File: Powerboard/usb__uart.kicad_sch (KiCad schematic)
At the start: 24 parts, among them IC2 CP2102, J8 USB_C_Receptacle_USB2.0, U10 RT9025-25GSP, U11 LTC4411

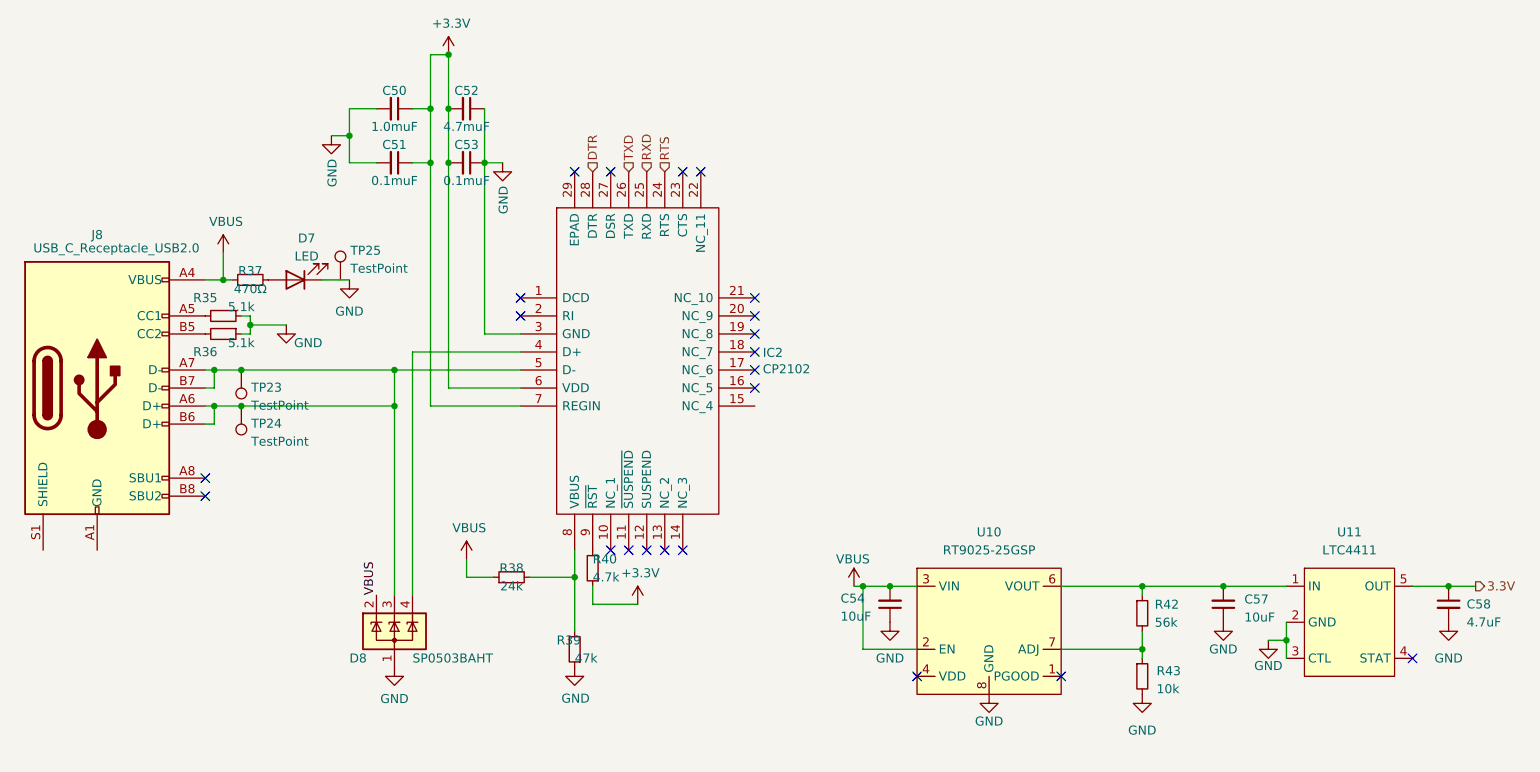
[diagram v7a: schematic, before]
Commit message: grouped components by circuit, done CAN transceiver layout.
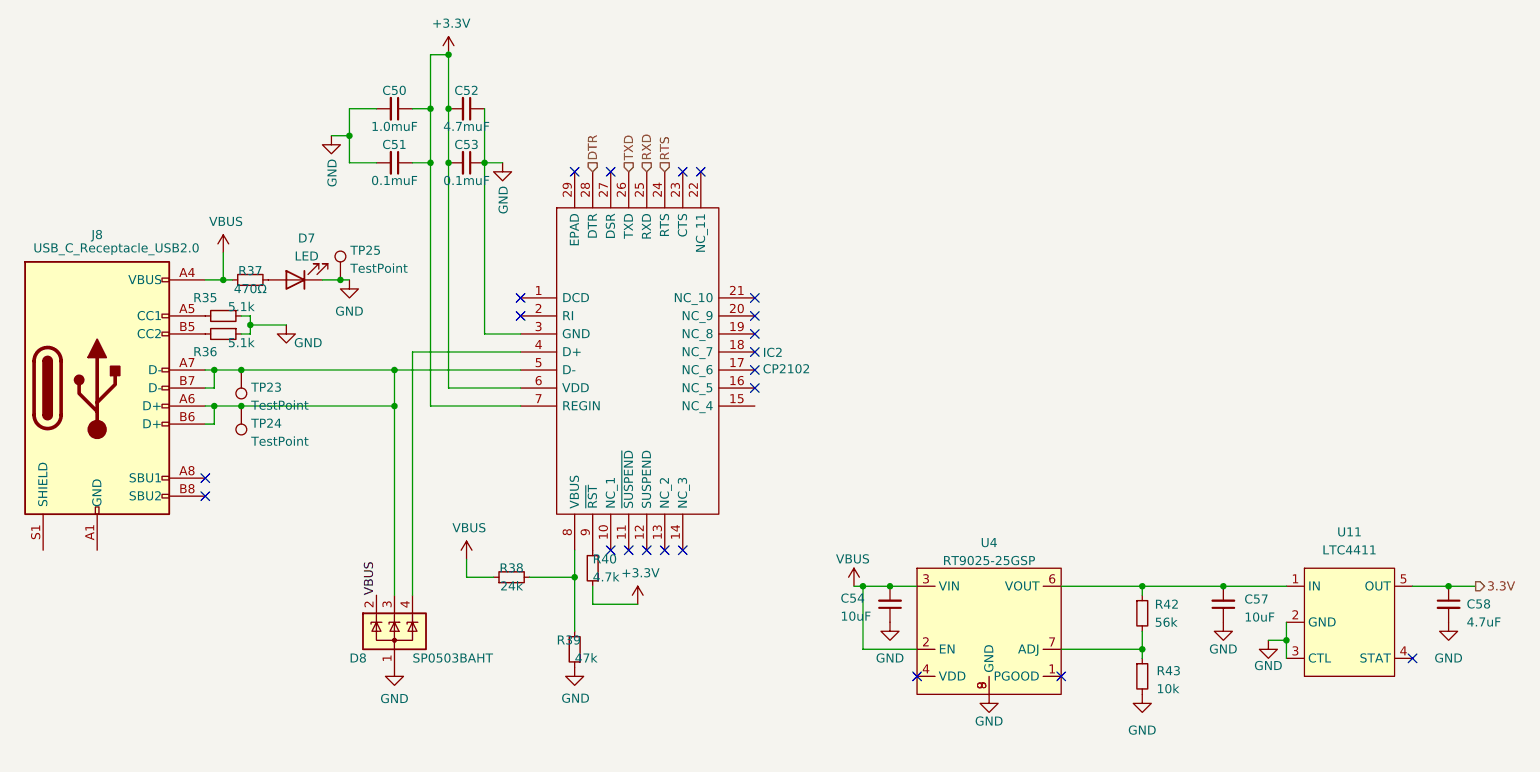
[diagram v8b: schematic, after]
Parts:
- removed U10: RT9025-25GSP, Package_SO:SOP-8_3.9x4.9mm_P1.27mm, symbol iclr:RT9025-25GSP
- added U4: RT9025-25GSP, iclr:SOIC127P599X175-9N, symbol iclr:RT9025-25GSP
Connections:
- net GND: now also TP25.1, U4.8 (GND), U4.9 (GND)
- net VBUS: now also U4.2 (EN), U4.3 (VIN)
- net at C57.2, R42.1, U11.1 (IN): now also U4.6 (VOUT)
- net at R42.2, R43.1: now also U4.7 (ADJ)
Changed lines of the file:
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@@
   (junction (at 115.57 58.42) (diameter 0) (color 0 0 0 0)
+  )
+  (junction (at 114.3 78.74) (diameter 0) (color 0 0 0 0)
   )
   (junction (at 270.51 121.92) (diameter 0) (color 0 0 0 0)
@@
   (no_connect (at 152.4 116.84))
   (no_connect (at 172.72 93.98))
+  (wire (pts (xy 114.3 78.74) (xy 115.57 78.74))
+    (stroke (width 0) (type default) (color 0 0 0 0))
+  )
   (wire (pts (xy 238.76 121.92) (xy 247.65 121.92))
     (stroke (width 0) (type default) (color 0 0 0 0))
@@
     (stroke (width 0) (type default) (color 0 0 0 0))
   )
-  (wire (pts (xy 111.76 78.74) (xy 115.57 78.74))
+  (wire (pts (xy 111.76 78.74) (xy 114.3 78.74))
     (stroke (width 0) (type default) (color 0 0 0 0))
   )
@@
   (symbol (lib_id "iclr:RT9025-25GSP") (at 205.74 120.65 0) (unit 1)
     (in_bom yes) (on_board yes) (fields_autoplaced)
-    (property "Reference" "U10" (id 0) (at 205.74 114.3 0))
-    (property "Value" "RT9025-25GSP" (id 1) (at 205.74 116.84 0))
-    (property "Footprint" "Package_SO:SOP-8_3.9x4.9mm_P1.27mm" (id 2) (at 205.74 115.57 0)
+    (property "Reference" "U4" (id 0) (at 205.74 115.8072 0))
+    (property "Value" "RT9025-25GSP" (id 1) (at 205.74 118.3441 0))
+    (property "Footprint" "iclr:SOIC127P599X175-9N" (id 2) (at 205.74 115.57 0)
       (effects (font (size 1.27 1.27)) hide)
     )
@@
     (pin "7")
     (pin "8")
+    (pin "9")
   )
   (symbol (lib_id "Device:C_Small") (at 270.51 124.46 0) (unit 1)
